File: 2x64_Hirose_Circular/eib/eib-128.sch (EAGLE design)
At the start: 52 parts

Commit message: Started applying revisions obtained from mechanical mockups
- This is the start of work toward rev 1.1 of Hirose 128 headstages.
- Headstages are designed to be semi-perminent. They are travel with the
  animal until it is sacraficed.
- Major changes to SPI interface board to get it working with Oat
  tracker and to conform with the semi-periment design decision.
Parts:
- SJ_A0, SJ_A1, SJ_B0, SJ_B1: device jonnew:SJ2_0201 -> jonnew:SJ2_0402
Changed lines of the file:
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@@
 <part name="SHLD_A0" library="jonnew" deviceset="GOLDPIN" device="_0.5ID_0.7OD" value="LRG_GP"/>
 <part name="SUPPLY1" library="jonnew" deviceset="GND" device=""/>
-<part name="SJ_A0" library="jonnew" deviceset="SJ2" device="_0201"/>
+<part name="SJ_A0" library="jonnew" deviceset="SJ2" device="_0402"/>
 <part name="AGND_A1" library="jonnew" deviceset="GOLDPIN" device="_0.5ID_0.7OD" value="LRG_GP"/>
 <part name="REF_A1" library="jonnew" deviceset="GOLDPIN" device="_0.5ID_0.7OD" value="LRG_GP"/>
@@
 <part name="SHLD_A1" library="jonnew" deviceset="GOLDPIN" device="_0.5ID_0.7OD" value="LRG_GP"/>
 <part name="SUPPLY2" library="jonnew" deviceset="GND" device=""/>
-<part name="SJ_A1" library="jonnew" deviceset="SJ2" device="_0201"/>
+<part name="SJ_A1" library="jonnew" deviceset="SJ2" device="_0402"/>
 <part name="FRAME1" library="jonnew" deviceset="FRAME" device=""/>
 <part name="U$2" library="jonnew" deviceset="DOCFIELD-GEN" device=""/>
 <part name="SHLD_B0" library="jonnew" deviceset="GOLDPIN" device="_0.5ID_0.7OD" value="LRG_GP"/>
 <part name="SUPPLY3" library="jonnew" deviceset="GND" device=""/>
-<part name="SJ_B0" library="jonnew" deviceset="SJ2" device="_0201"/>
+<part name="SJ_B0" library="jonnew" deviceset="SJ2" device="_0402"/>
 <part name="SHLD_B1" library="jonnew" deviceset="GOLDPIN" device="_0.5ID_0.7OD" value="LRG_GP"/>
 <part name="SUPPLY4" library="jonnew" deviceset="GND" device=""/>
-<part name="SJ_B1" library="jonnew" deviceset="SJ2" device="_0201"/>
+<part name="SJ_B1" library="jonnew" deviceset="SJ2" device="_0402"/>
 <part name="AGND_B0" library="jonnew" deviceset="GOLDPIN" device="_0.5ID_0.7OD" value="LRG_GP"/>
 <part name="REF_B1" library="jonnew" deviceset="GOLDPIN" device="_0.5ID_0.7OD" value="LRG_GP"/>

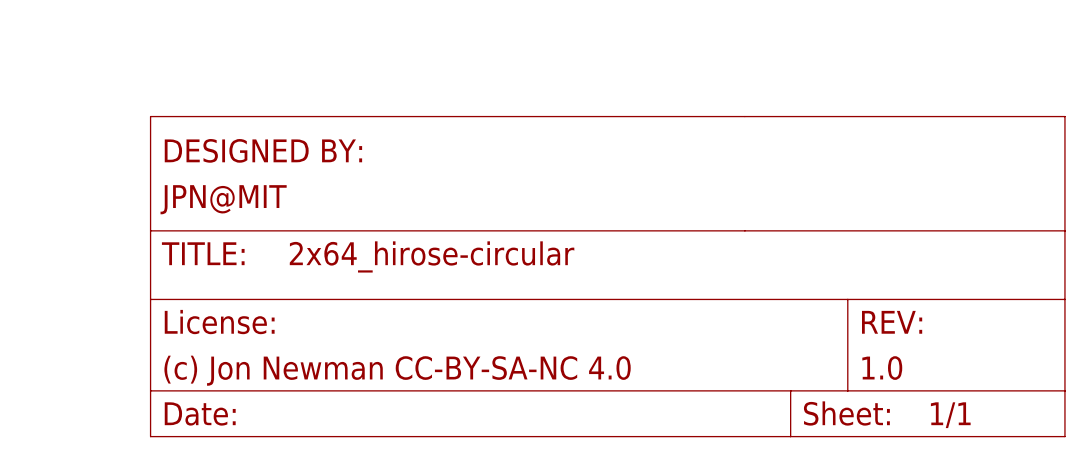
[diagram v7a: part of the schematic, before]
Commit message: Nearly finished with revision 1.1 of Hirose-128 headstage.
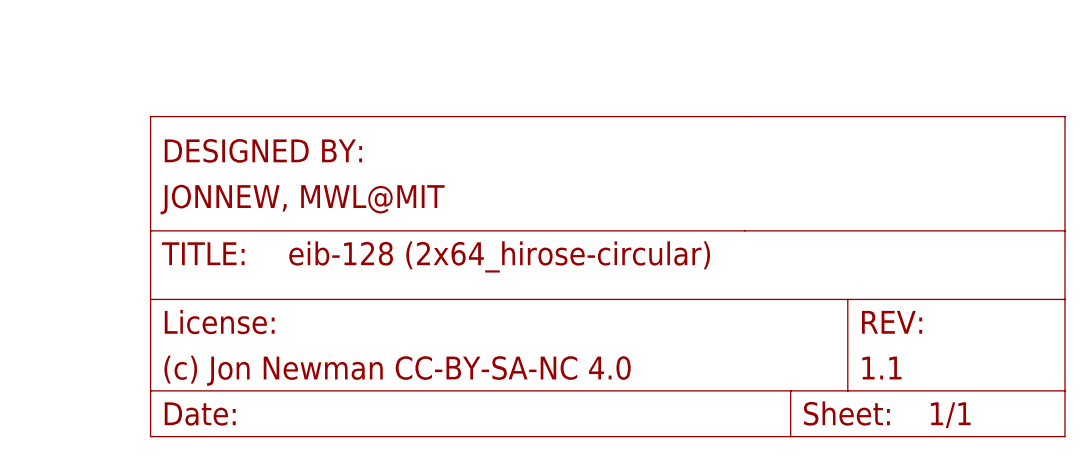
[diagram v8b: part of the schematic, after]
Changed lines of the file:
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@@
 <schematic xreflabel="%F%N/%S.%C%R" xrefpart="/%S.%C%R">
 <attributes>
-<attribute name="DESIGNER" value="JPN@MIT"/>
-<attribute name="DESIGN_NAME" value="2x64_hirose-circular"/>
+<attribute name="DESIGNER" value="JONNEW, MWL@MIT"/>
+<attribute name="DESIGN_NAME" value="eib-128 (2x64_hirose-circular)"/>
 <attribute name="LICENSE" value="(c) Jon Newman CC-BY-SA-NC 4.0"/>
-<attribute name="REVISION" value="1.0"/>
+<attribute name="REVISION" value="1.1"/>
 </attributes>
 <variantdefs>
